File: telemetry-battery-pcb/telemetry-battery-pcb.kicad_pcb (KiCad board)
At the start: 2 copper layers, 95 x 65 mm, 110 parts, among them J1 Network Connector, J2 STDC14, J3 CONN_360410_MZC, J4 DS18B20, J5 CONN_360410_MZC, Q1 NMOS, Q2 PMOS, Q4 NMOS, SW1 SW_Push, U1 LD39050PU33R, U2 STM32G474RBT6, U3 SN65HVD230, U4 LTC2944, U5 XR76208, U6 M24C02-WMN, U7 Tps1htc, U8 DS2484R, Y1 8MHz

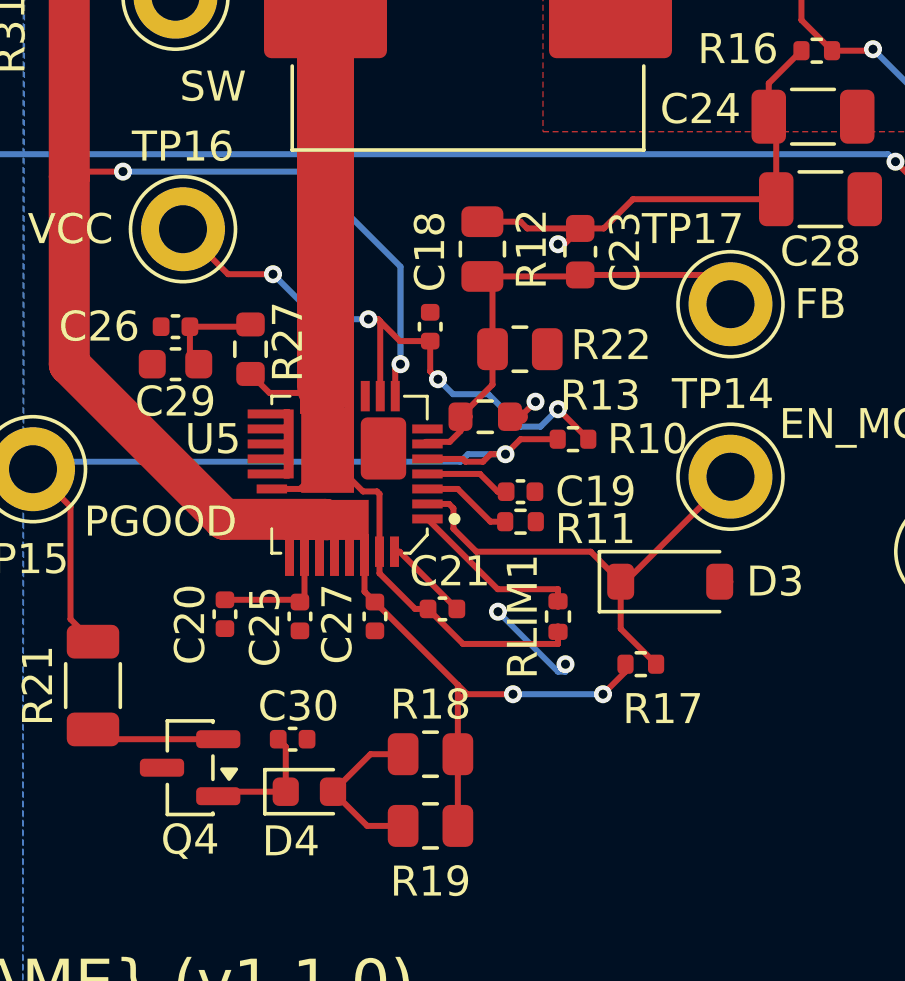
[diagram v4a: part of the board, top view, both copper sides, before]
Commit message: telemetry-battery-pcb: components numbers JLCPCB and footprints change
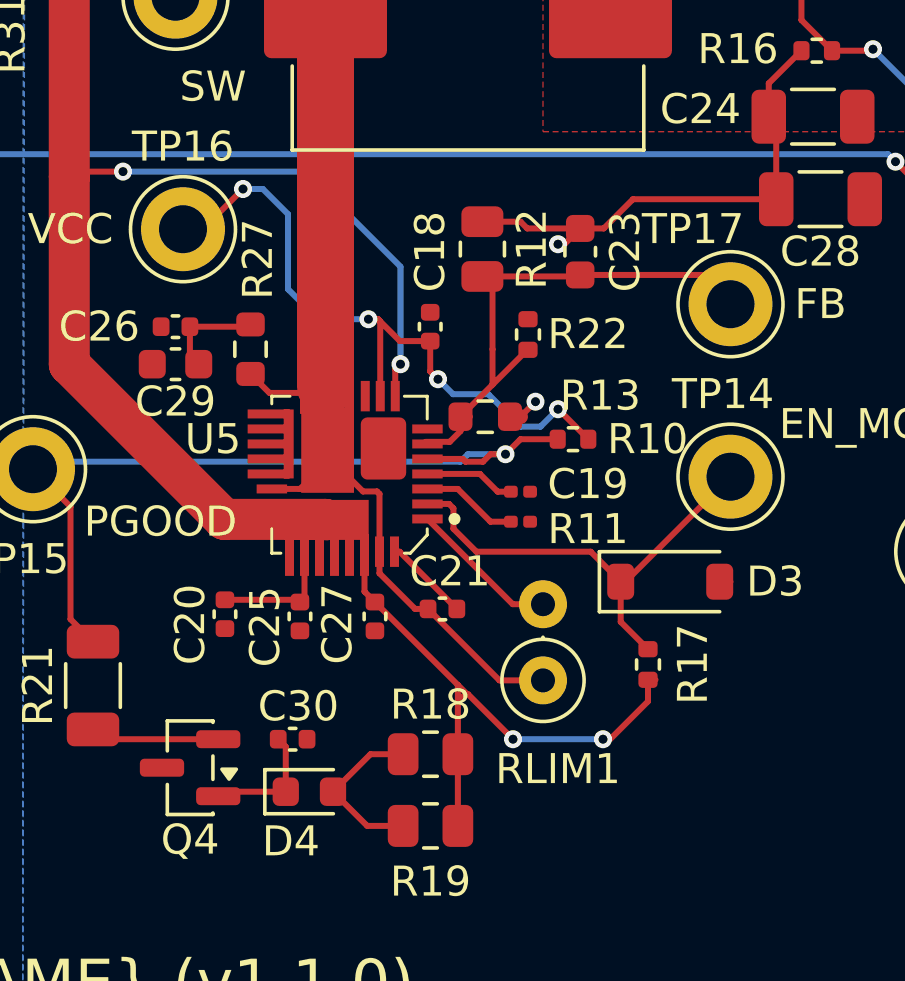
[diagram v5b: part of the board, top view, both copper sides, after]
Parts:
- C19: footprint Capacitor_SMD:C_0402_1005Metric -> Capacitor_SMD:C_0201_0603Metric
- C25: value 0.1u -> 100n
- R11: footprint Resistor_SMD:R_0402_1005Metric -> Resistor_SMD:R_0201_0603Metric
- R22: footprint Resistor_SMD:R_0805_2012Metric -> Resistor_SMD:R_0402_1005Metric
- RLIM1: footprint Resistor_SMD:R_0402_1005Metric -> Resistor_THT:R_Axial_DIN0207_L6.3mm_D2.5mm_P2.54mm_Vertical
- moved RLIM1 2.19 mm to (116.5, 73.0)
- moved R22 0.56 mm to (116.0, 61.5), turned to 90 degrees
- moved R17 0.24 mm to (120.0, 72.5), turned to -90 degrees
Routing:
- net GND: track 4.08 -> 0.75 mm, vias 2 -> 0
- net /VCC: track 20.1 -> 22.7 mm
- net +24V: track 94.0 -> 95.9 mm
- net /FB: track 16.2 -> 17.8 mm
- net Net-(U5-ILIM): track 5.91 -> 5.03 mm
- net /EN_MODE: track 16.3 -> 15.7 mm
- net /SW: track 35.6 -> 35.0 mm

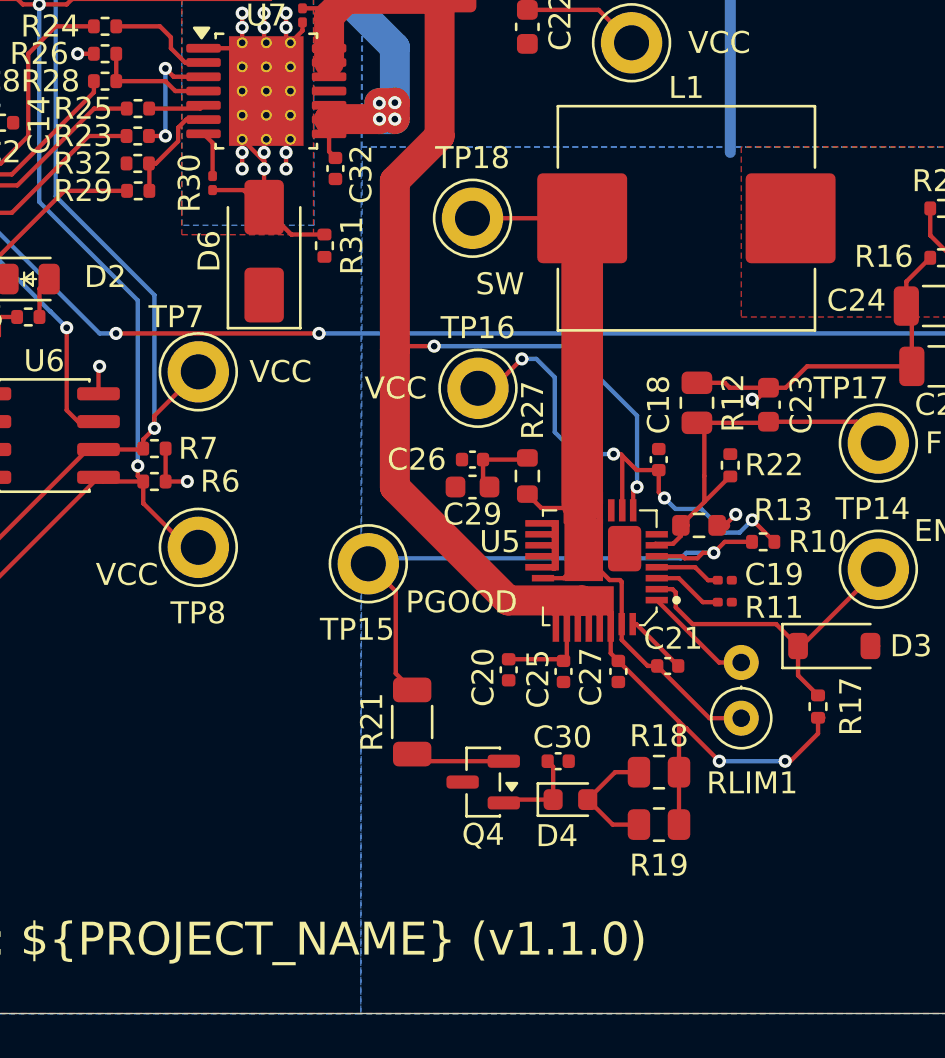
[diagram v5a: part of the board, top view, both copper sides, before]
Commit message: telemetry-battery-pcb: Changes on footprints Rlim and R30
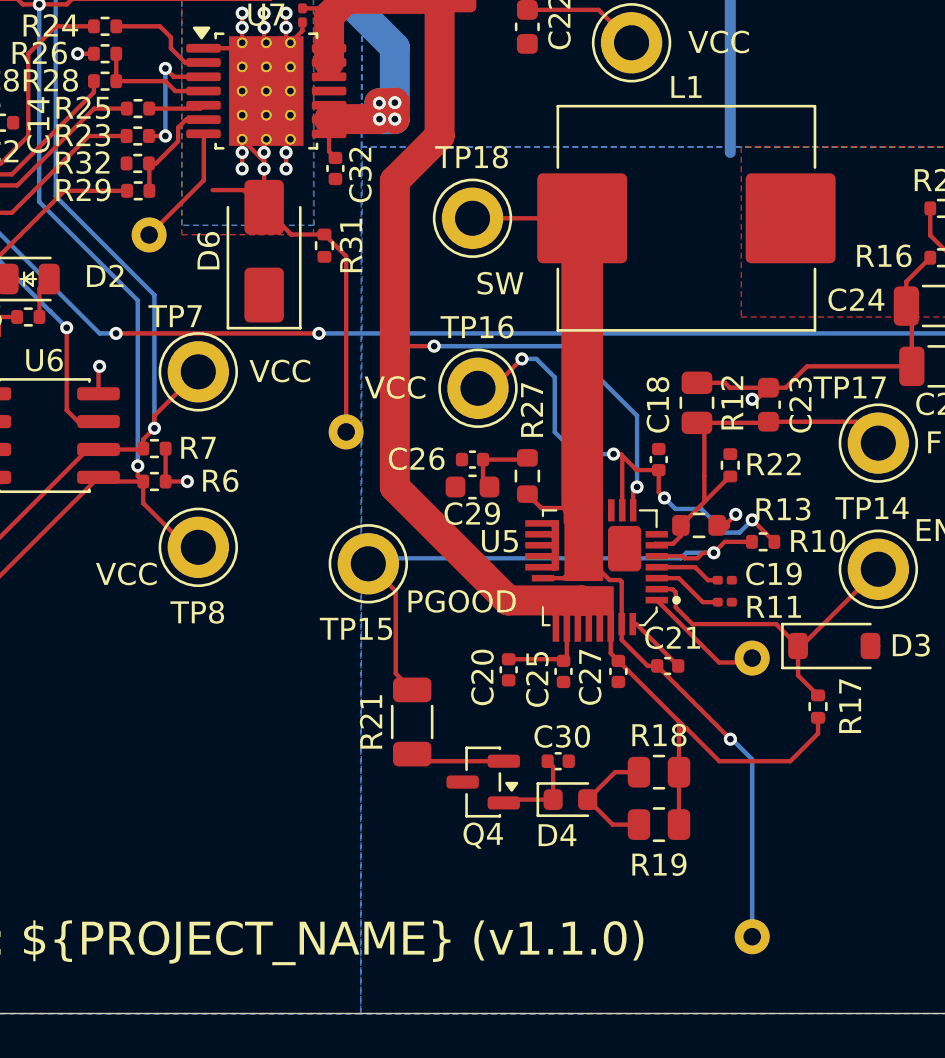
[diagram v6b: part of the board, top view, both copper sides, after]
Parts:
- R30: footprint Resistor_SMD:R_0201_0603Metric -> Resistor_THT:R_Axial_DIN0309_L9.0mm_D3.2mm_P12.70mm_Horizontal; moved to B.Cu
- RLIM1: footprint Resistor_THT:R_Axial_DIN0207_L6.3mm_D2.5mm_P2.54mm_Vertical -> Resistor_THT:R_Axial_DIN0309_L9.0mm_D3.2mm_P12.70mm_Horizontal; moved to B.Cu
- moved R30 12.9 mm to (98.5, 60.0), turned to 135 degrees
- moved RLIM1 9.97 mm to (117.0, 83.0)
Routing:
- net /GND_L: track 20.0 -> 29.4 mm
- net /SW: track 35.0 -> 44.3 mm, vias 0 -> 1
- net Net-(U7-ILIM): track 2.10 -> 5.65 mm
- net +24V: track 95.9 -> 96.1 mm, vias 4 -> 2

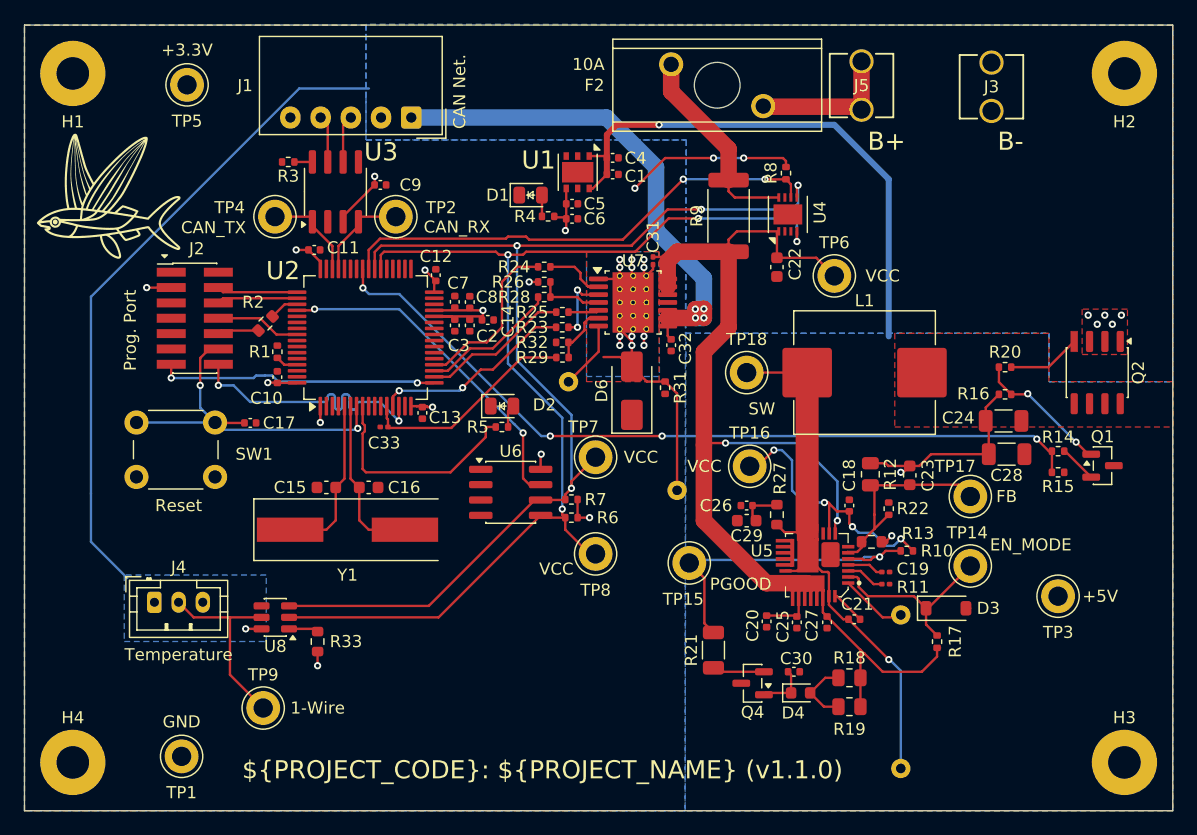
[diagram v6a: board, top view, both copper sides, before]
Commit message: telemetry-battery-pcb: add fixes for template
- Added an extra footprint for a fuse
- Increased LED resistor value
- Rounded board corners
- Changed temperature sensor connector for horizontal version (not from
  template)
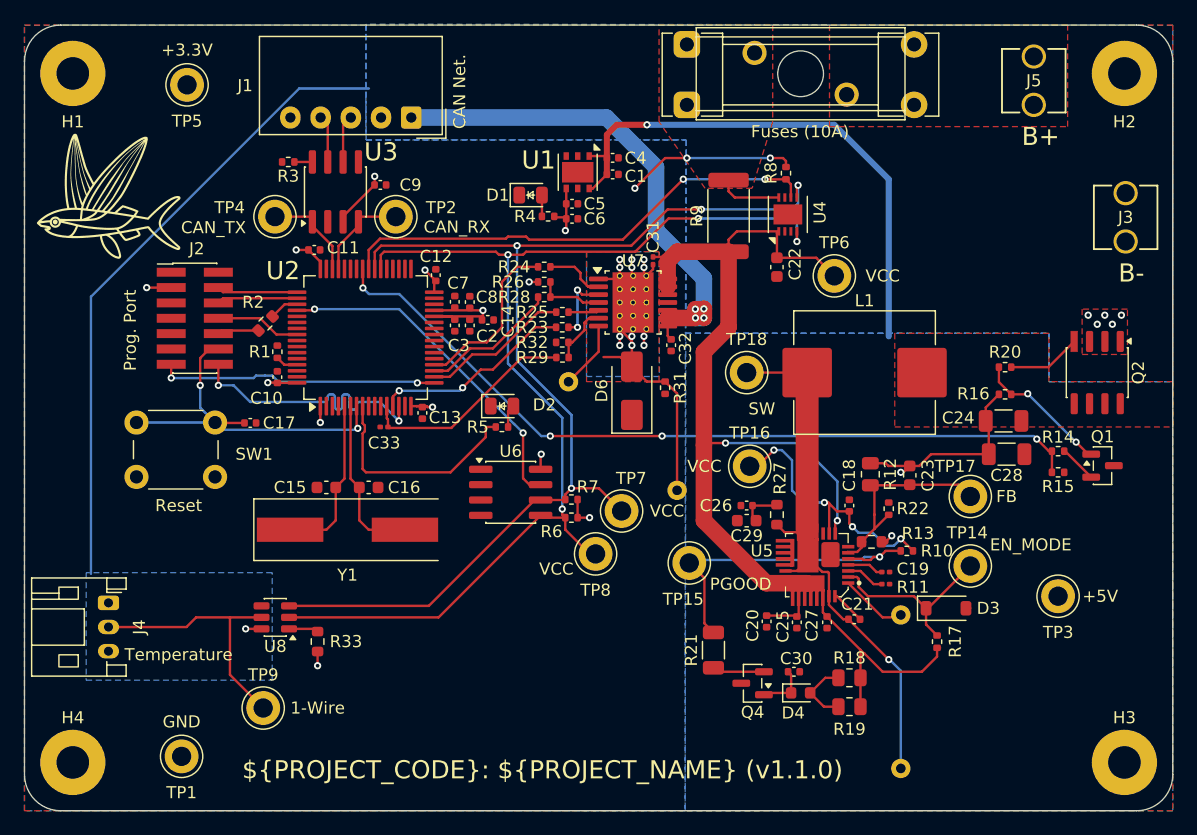
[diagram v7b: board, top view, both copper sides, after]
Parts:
- added F1: 10A, Fuse:Fuseholder_Clip-5x20mm_Littelfuse_111_Lateral_P18.80x5.00mm_D1.17mm_Horizontal, F.Cu at (99.3, 23.1)
- J4: footprint Connector_JST:JST_PH_B3B-PH-K_1x03_P2.00mm_Vertical -> Connector_JST:JST_PH_S3B-PH-K_1x03_P2.00mm_Horizontal
- R4, R5: value 100 -> 1k
- moved J3 15.5 mm to (135.6, 35.4)
- moved J5 14.3 mm to (128.0, 24.1)
- moved F2 6.97 mm to (108.7, 25.5)
- moved TP7 4.94 mm to (93.9, 61.7)
- moved J4 3.80 mm to (51.5, 69.3), turned to -90 degrees
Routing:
- net /batt+: track 12.3 -> 0.00 mm
- net Net-(U4-SENSE-): track 16.8 -> 5.29 mm
- net /ONE_WIRE: track 16.0 -> 21.6 mm
- net /5V_net: track 56.5 -> 54.9 mm
- net /SDA: track 93.6 -> 95.1 mm
- added copper zone on F.Cu, net /batt+
- added copper zone on F.Cu, net Net-(U4-SENSE-)
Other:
- outline, holes or cut-outs redrawn
- board text added: "Fuses (10A)"

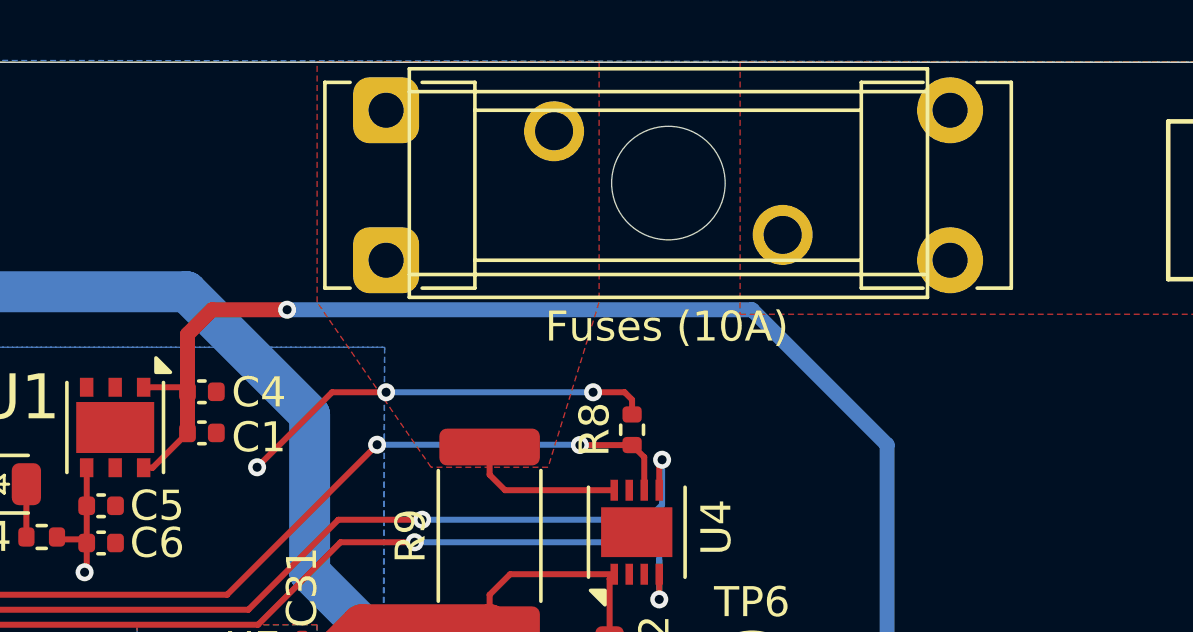
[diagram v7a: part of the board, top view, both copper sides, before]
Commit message: telemetry-battery-pcb: add combined fuseholder footprint
This gets rid of all remaining DRC warnings and makes the schematic a
little clearer.
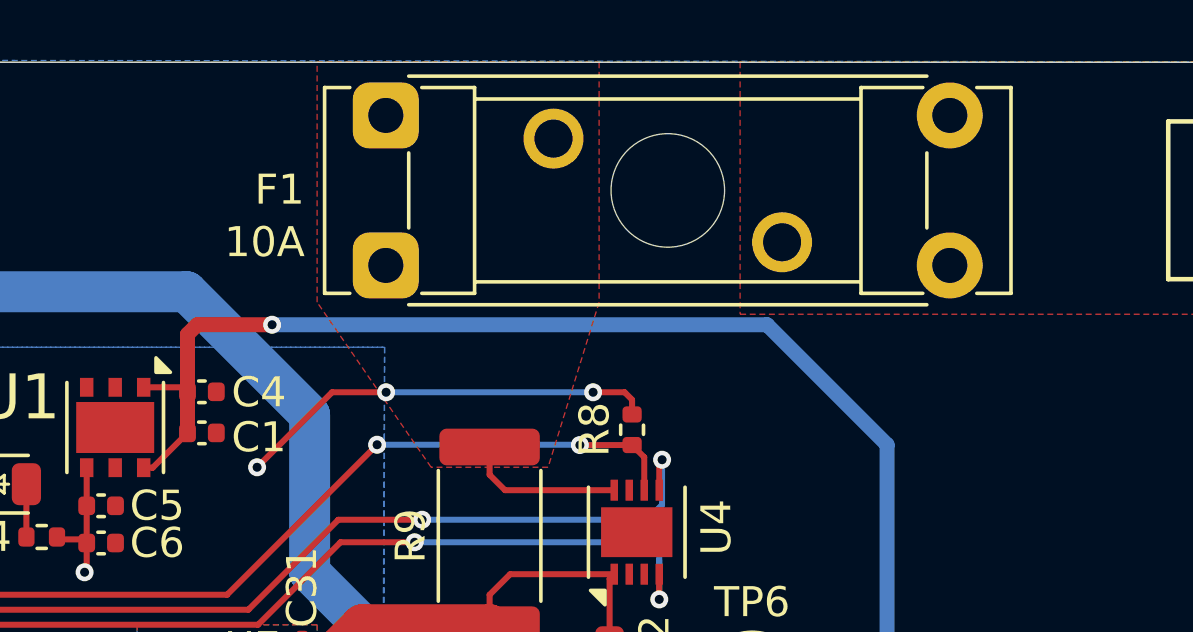
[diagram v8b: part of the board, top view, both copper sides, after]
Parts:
- removed F2: 10A, Exocet:Fuse_Holder_Littelfuse_01530008
- F1: footprint Fuse:Fuseholder_Clip-5x20mm_Littelfuse_111_Lateral_P18.80x5.00mm_D1.17mm_Horizontal -> Exocet:Fuseholder_Littelfuse_Combined
- moved F1 9.76 mm to (108.7, 25.8)
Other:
- board text removed: "Fuses (10A)"
